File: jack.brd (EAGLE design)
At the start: 100 x 80 mm, 30 parts, among them IC1 NUF2221W1T2G, IC2 ATSAMD21G18, IC3 LDO, SW1 SPST3.5X6MM, X1 TSX-3225 24.0000MF10Z-C3

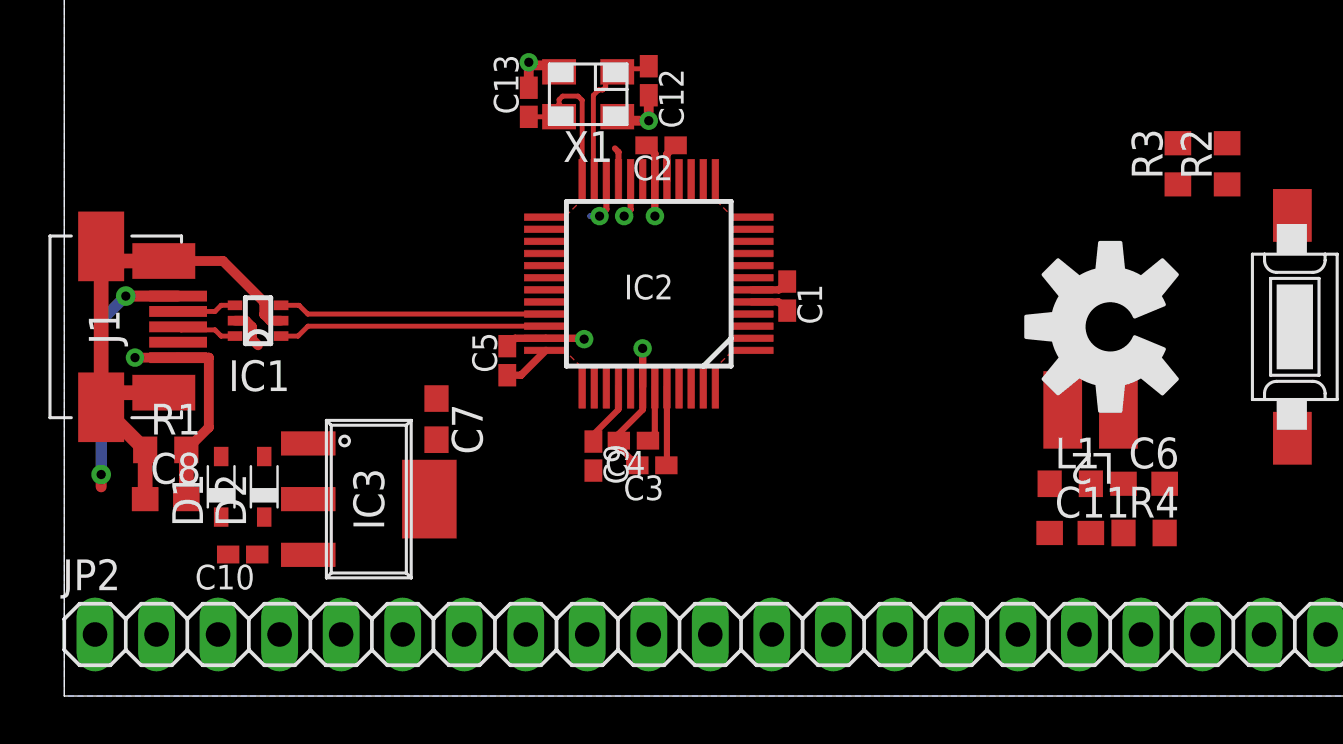
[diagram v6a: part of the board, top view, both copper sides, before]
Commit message: Started power signals layout
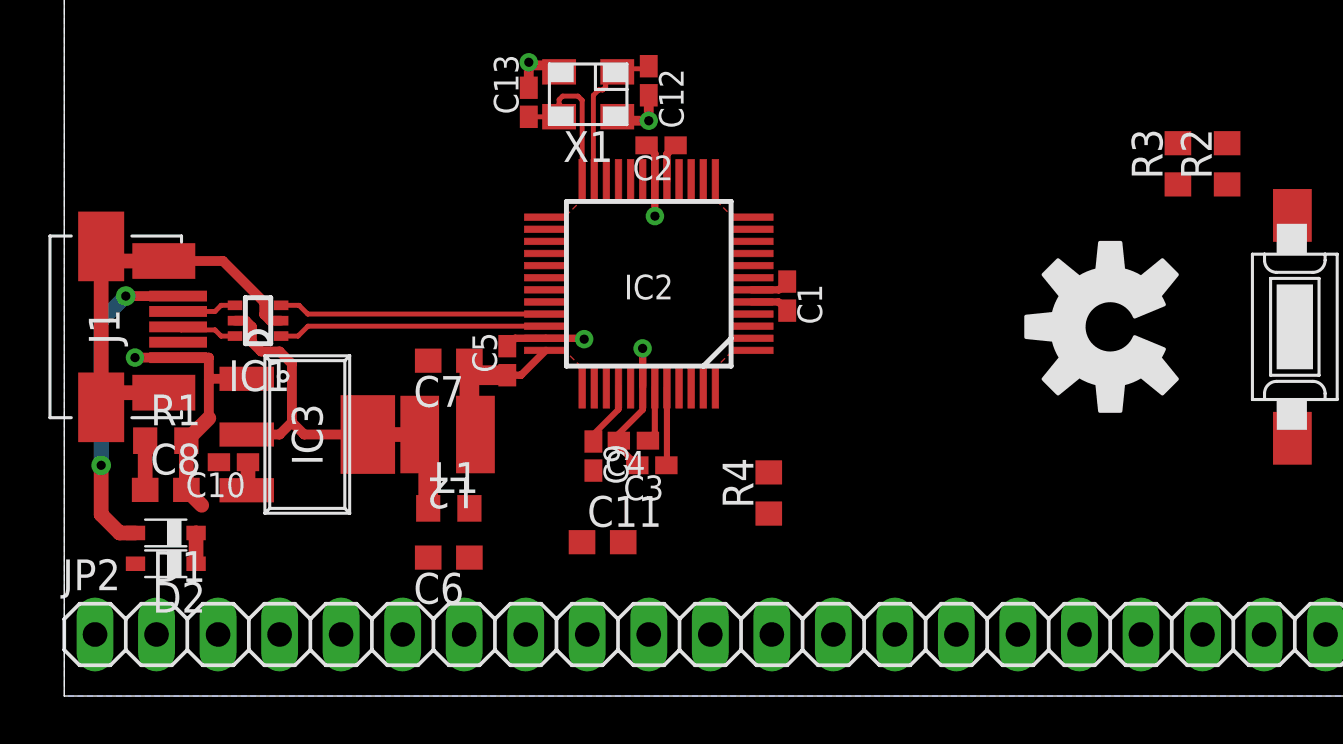
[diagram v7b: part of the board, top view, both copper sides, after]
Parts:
- moved C6 28.9 mm to (15.9, 5.71), turned to 180 degrees
- moved L2 26.6 mm to (15.9, 10.8)
- moved L1 25.7 mm to (15.9, 7.75)
- moved C11 19.3 mm to (22.2, 6.35)
- moved R4 15.6 mm to (29.1, 8.38), turned to 90 degrees
- moved D2 5.16 mm to (4.19, 5.46), turned to 180 degrees
- moved C10 3.83 mm to (6.99, 9.65)
- moved IC3 3.68 mm to (10.0, 10.8)
- moved D1 2.98 mm to (4.19, 6.73), turned to 180 degrees
- moved C7 2.47 mm to (15.9, 13.8), turned to 180 degrees
- moved C8 0.38 mm to (4.19, 8.51)
- moved R1 0.38 mm to (4.19, 10.5)
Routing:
- net VDD: track 1.67 -> 16.6 mm
- net VDDF: track 6.87 -> 11.7 mm
- net VBUS: track 10.5 -> 13.5 mm
- net LDOIN: track 0.00 -> 2.49 mm
- net SH_GND: track 22.5 -> 20.1 mm
- net GND: track 26.3 -> 28.4 mm
- net 22: track 1.95 -> 0.00 mm, vias 1 -> 0
- net 20: track 1.57 -> 0.00 mm, vias 1 -> 0
- net 21: track 1.40 -> 0.00 mm

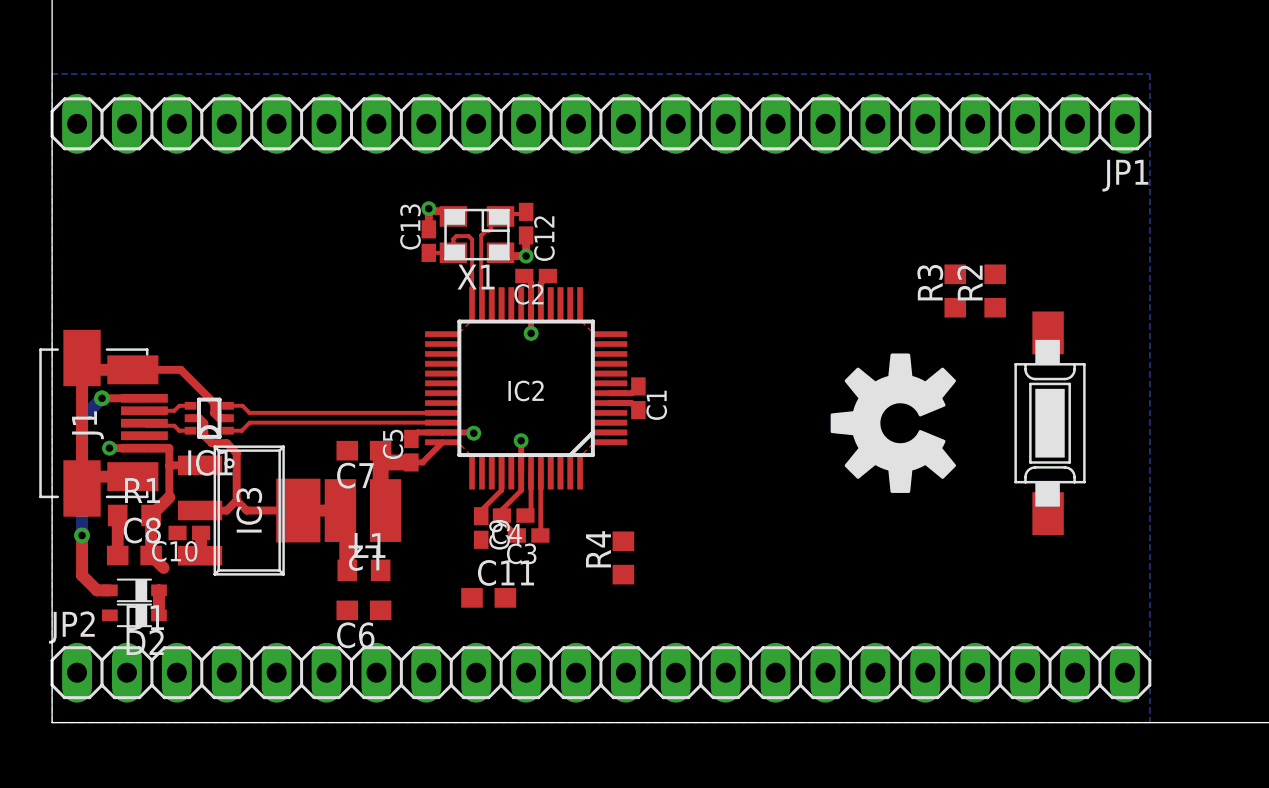
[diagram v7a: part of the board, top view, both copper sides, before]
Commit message: :thumbsup: Updated mcu pins/breakout header map
I'm mapping the pins of the ATSAM21D to the breakout header in a way
that reduces airwires length on the PCB, thus easing the layout process
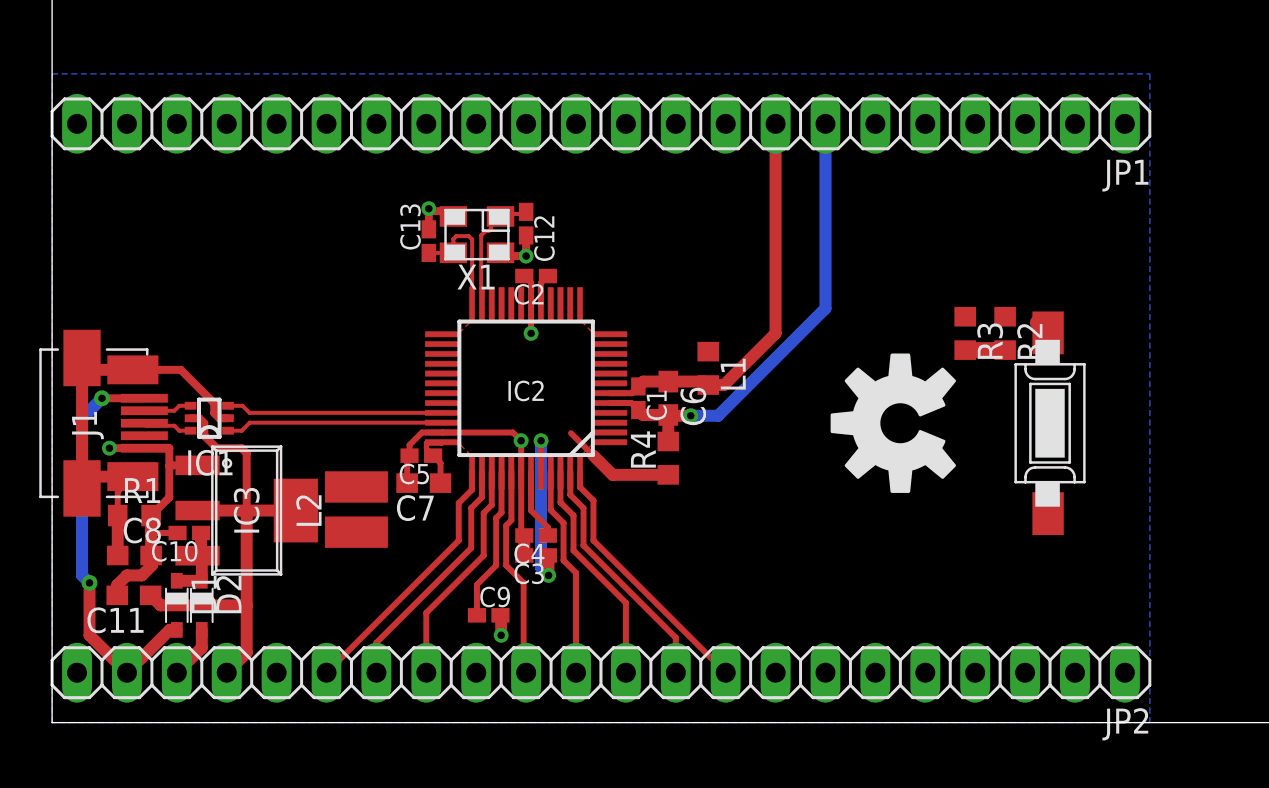
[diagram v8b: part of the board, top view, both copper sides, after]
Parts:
- moved L1 20.3 mm to (33.4, 18.0), turned to 270 degrees
- moved C6 18.9 mm to (31.4, 16.5), turned to 270 degrees
- moved C11 18.1 mm to (4.17, 6.48), turned to 180 degrees
- moved R4 5.57 mm to (31.4, 13.5)
- moved C9 4.46 mm to (22.2, 5.46), turned to 0 degrees
- moved D2 3.47 mm to (7.62, 5.97), turned to 270 degrees
- moved C7 3.47 mm to (18.9, 12.2)
- moved D1 2.29 mm to (6.35, 5.97), turned to 270 degrees
- moved R2 2.22 mm to (48.5, 19.8), turned to 270 degrees
- moved R3 2.22 mm to (46.5, 19.8), turned to 270 degrees
- moved C4 1.53 mm to (24.6, 9.53)
- moved C3 1.09 mm to (24.6, 8.51)
- moved C5 0.57 mm to (18.8, 13.6), turned to 180 degrees
- moved L2 0.38 mm to (15.5, 10.8), turned to 90 degrees
- moved IC3 0.13 mm to (9.91, 10.8)
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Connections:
- net !RESET: now also JP2.14; no longer JP2.12
- net 37: now also JP2.17; no longer JP2.9
- net 38: now also JP2.16; no longer JP2.10
- net 39: now also JP2.15; no longer JP2.11
- net 47: now also JP2.10; no longer JP2.16
- net 48: now also JP2.9; no longer JP2.17
- net SWCLK: now also JP2.12; no longer JP2.14
- net SWDIO: now also JP2.11; no longer JP2.15
- net VDD: no longer R3.1
- net VDDF: now also R3.1
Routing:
- net GNDANA: track 1.61 -> 24.3 mm, vias 0 -> 1
- net VDDANA: track 1.61 -> 20.5 mm
- net GND: track 28.4 -> 44.2 mm
- net 48: track 0.00 -> 13.3 mm
- net 37: track 0.00 -> 13.3 mm
- net 47: track 0.00 -> 12.5 mm
- net 38: track 0.00 -> 12.5 mm
- net SWDIO: track 0.00 -> 11.6 mm
- net 39: track 0.00 -> 11.6 mm
- net SWCLK: track 0.00 -> 10.8 mm
- net 41: track 0.00 -> 10.8 mm
- net VDD: track 16.6 -> 25.7 mm
- net VBUS: track 13.5 -> 21.1 mm
- net !RESET: track 2.69 -> 9.86 mm
- net VDDF: track 11.7 -> 14.4 mm, vias 0 -> 2
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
